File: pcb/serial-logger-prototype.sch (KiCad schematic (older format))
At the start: 52 parts, among them J1 Conn_ARM_JTAG_SWD_10, J2 Conn_01x04_Female, J3 Conn_01x04_Female, J4 Conn_01x03_Male, SW1 Rotary_Encoder_Switch_DualLED, SW2 SW_SPDT, U1 STM32G070KBT6, U2 74LVC3G17, U3 TLV70228_SOT23-5, U4 sn74lv1t34, U5 TLV61046ADB, U6 sn74lv1t34

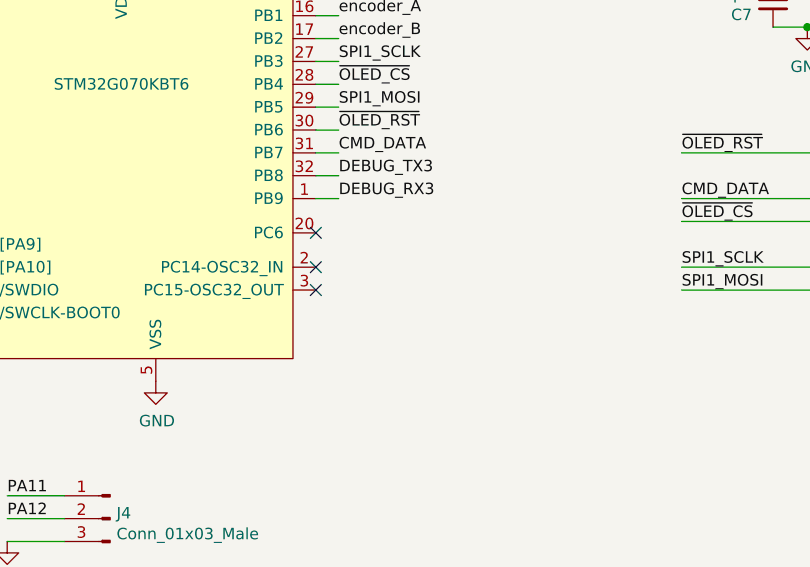
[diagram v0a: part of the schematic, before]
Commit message: Add note about PC13-15
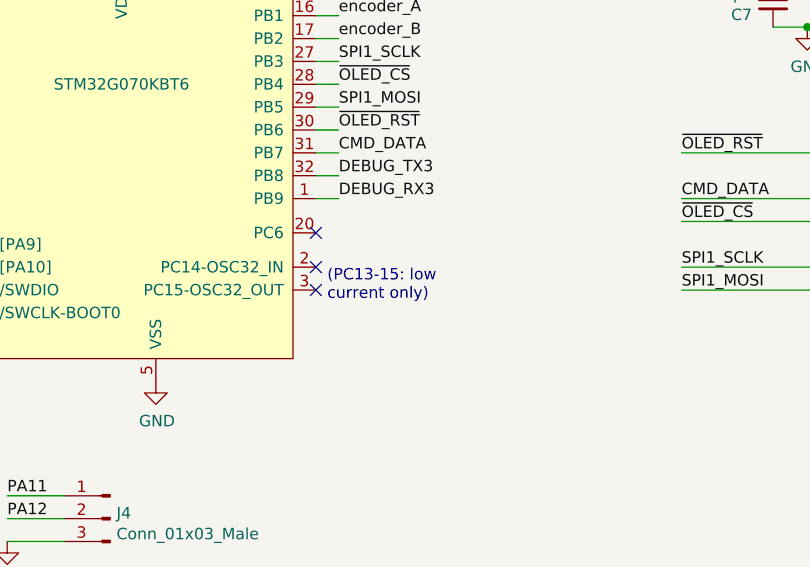
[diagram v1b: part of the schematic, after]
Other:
- note added: "(PC13-15: low\ncurrent only)"
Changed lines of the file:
@@
 	-1   0    0    -1
 $EndComp
+Text Notes 4850 3300 0    50   ~ 0
+(PC13-15: low\ncurrent only)
 $EndSCHEMATC

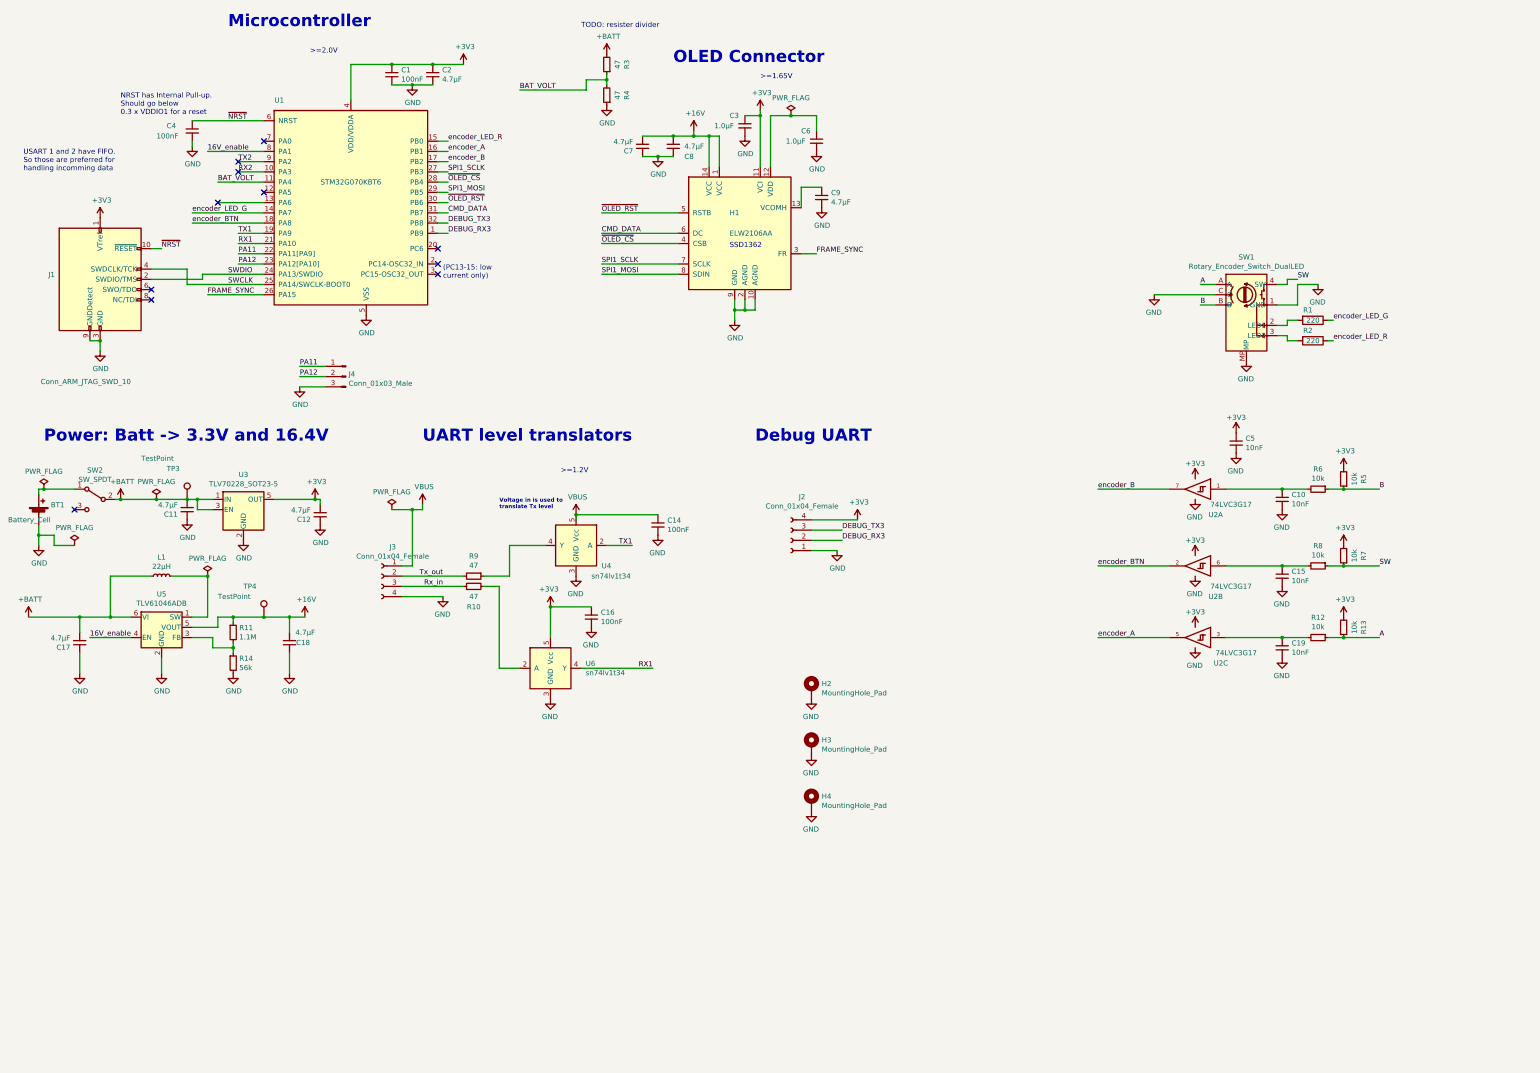
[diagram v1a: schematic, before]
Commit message: Schematics: implement BATT_VOLT, shuffle schematics blocks around
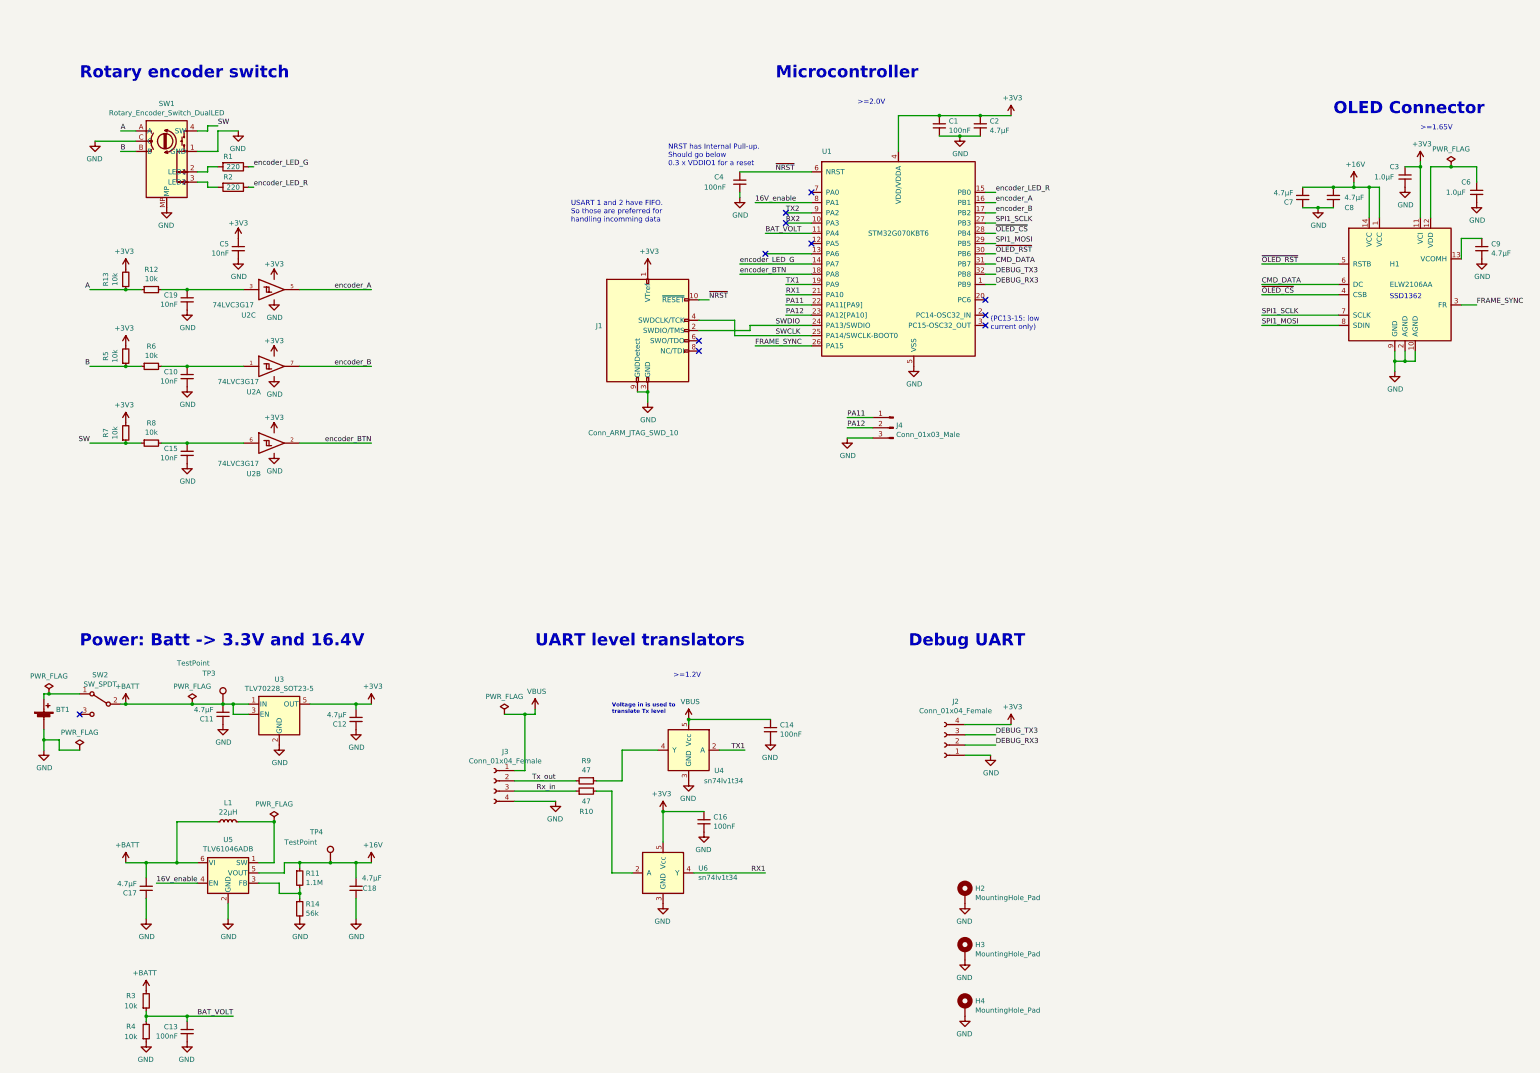
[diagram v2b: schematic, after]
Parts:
- added C13: 100nF, Capacitor_SMD:C_0402_1005Metric, symbol Device:C_Small
- C4: Reason (none) -> prevent parasitic resets (see datasheet 5.3.15)
- R3, R4: value 47 -> 10k
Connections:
- net BAT_VOLT: now also C13.1
- net GND: now also C13.2
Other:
- note added: "Rotary encoder switch"
- note removed: "TODO: resister divider"
- moved on the sheet: BT1, C1, C10, C11, C12, C14, C15, C16, C17, C18, C19, C2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

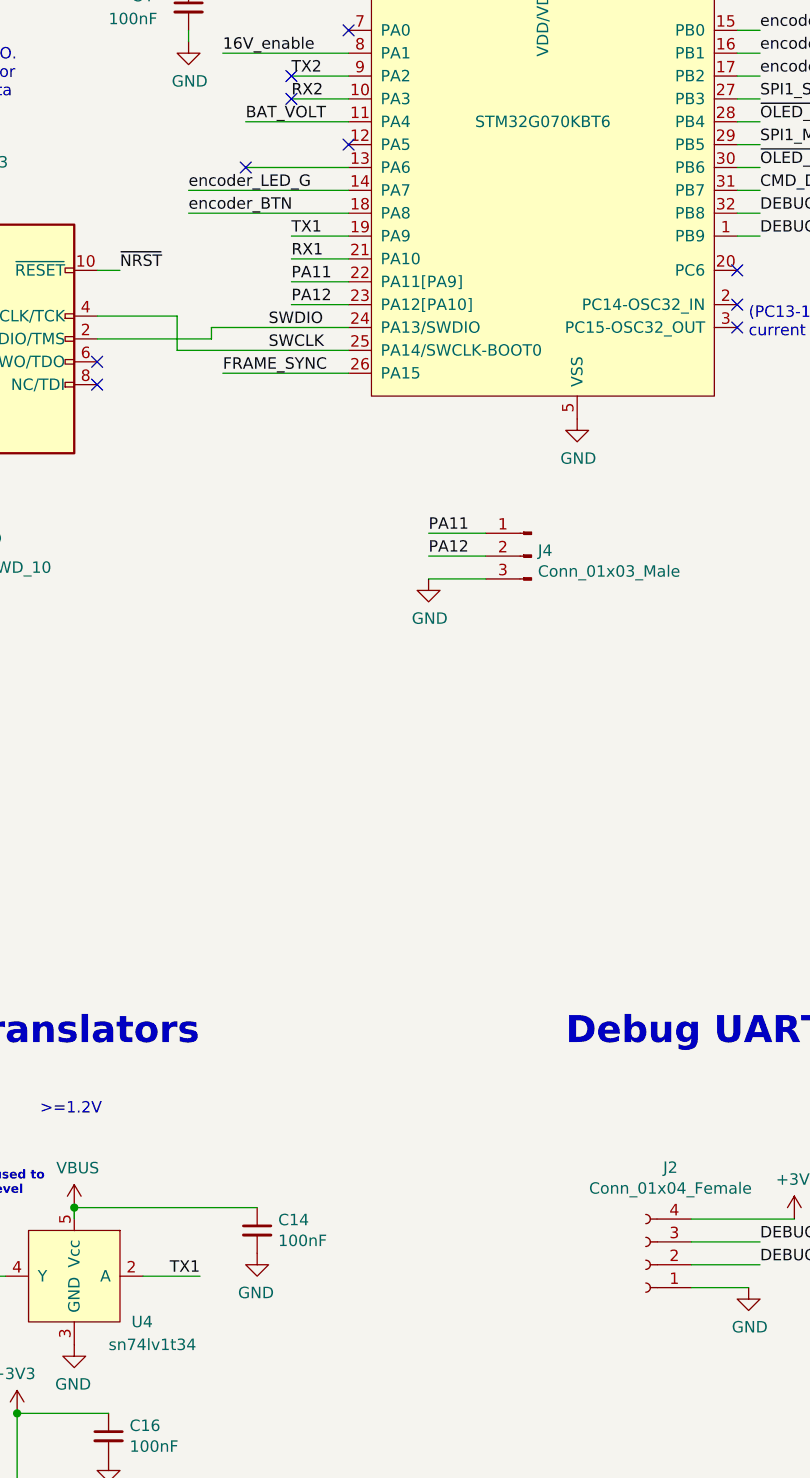
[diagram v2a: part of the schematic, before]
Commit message: PCB: cleanup layout, optimize for 3d enclosure
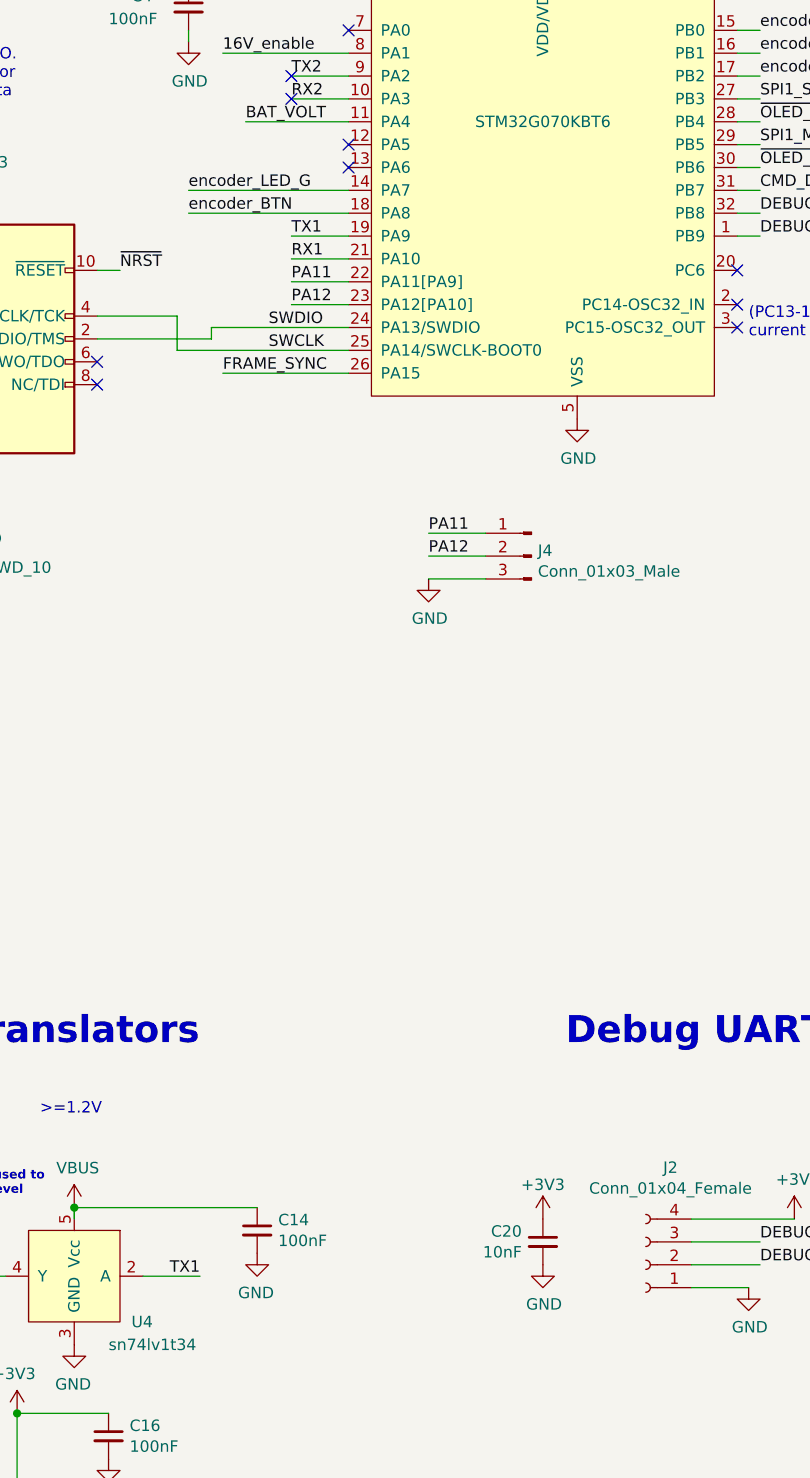
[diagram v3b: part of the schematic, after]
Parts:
- added C20: 10nF, Capacitor_SMD:C_0402_1005Metric, symbol Device:C_Small
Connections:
- net +3V3: now also C20.1
- net GND: now also C20.2
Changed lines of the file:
@@
 Text Label 10250 2950 0    50   ~ 0
 SPI1_MOSI
-Wire Wire Line
-	8000 3050 8450 3050
 $Comp
 L Device:C_Small C4
@@
 Wire Wire Line
 	7750 2450 7750 2500
-NoConn ~ 8000 3050
+NoConn ~ 8450 3050
 $Comp
 L power:GND #PWR035
@@
 	-1   0    0    -1
 $EndComp
+$Comp
+L Device:C_Small C20
+U 1 1 5E5CE5CC
+P 9300 7750
+F 0 "C20" H 9392 7796 50  0000 L CNN
+F 1 "10nF" H 9392 7705 50  0000 L CNN
+F 2 "Capacitor_SMD:C_0402_1005Metric" H 9300 7750 50  0001 C CNN
+F 3 "~" H 9300 7750 50  0001 C CNN
+	1    9300 7750
+	-1   0    0    -1
+$EndComp
+$Comp
+L power:GND #PWR0108
+U 1 1 5E5CE5D2
+P 9300 7850
+F 0 "#PWR0108" H 9300 7600 50  0001 C CNN
+F 1 "GND" H 9305 7677 50  0000 C CNN
+F 2 "" H 9300 7850 50  0001 C CNN
+F 3 "" H 9300 7850 50  0001 C CNN
+	1    9300 7850
+	1    0    0    -1
+$EndComp
+$Comp
+L power:+3V3 #PWR0109
+U 1 1 5E5CE5D8
+P 9300 7650
+F 0 "#PWR0109" H 9300 7500 50  0001 C CNN
+F 1 "+3V3" H 9300 7800 50  0000 C CNN
+F 2 "" H 9300 7650 50  0001 C CNN
+F 3 "" H 9300 7650 50  0001 C CNN
+	1    9300 7650
+	-1   0    0    -1
+$EndComp

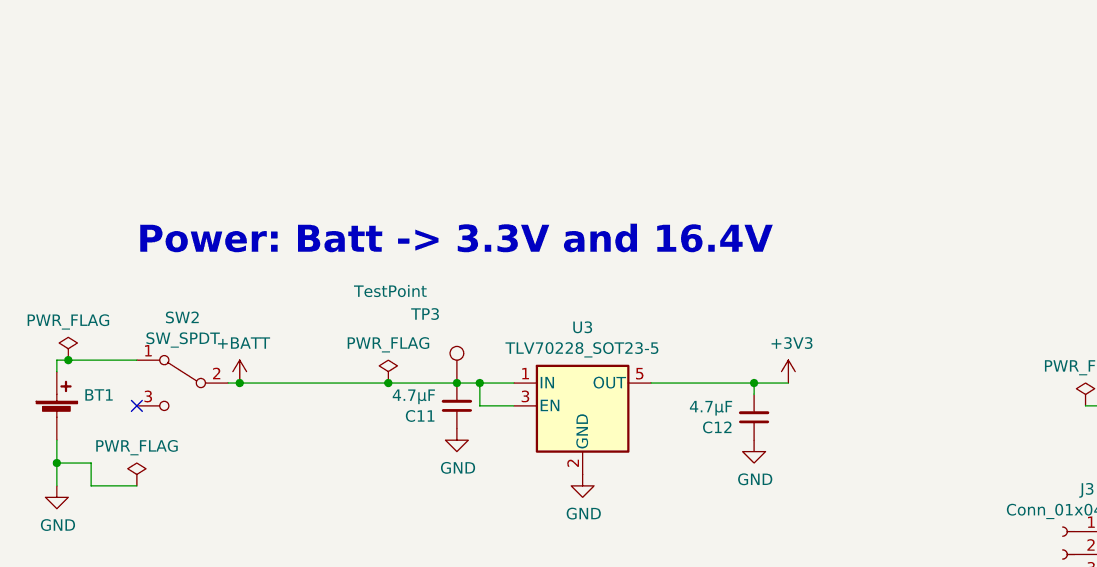
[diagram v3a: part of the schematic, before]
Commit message: PCB: tweak placements + silk screen
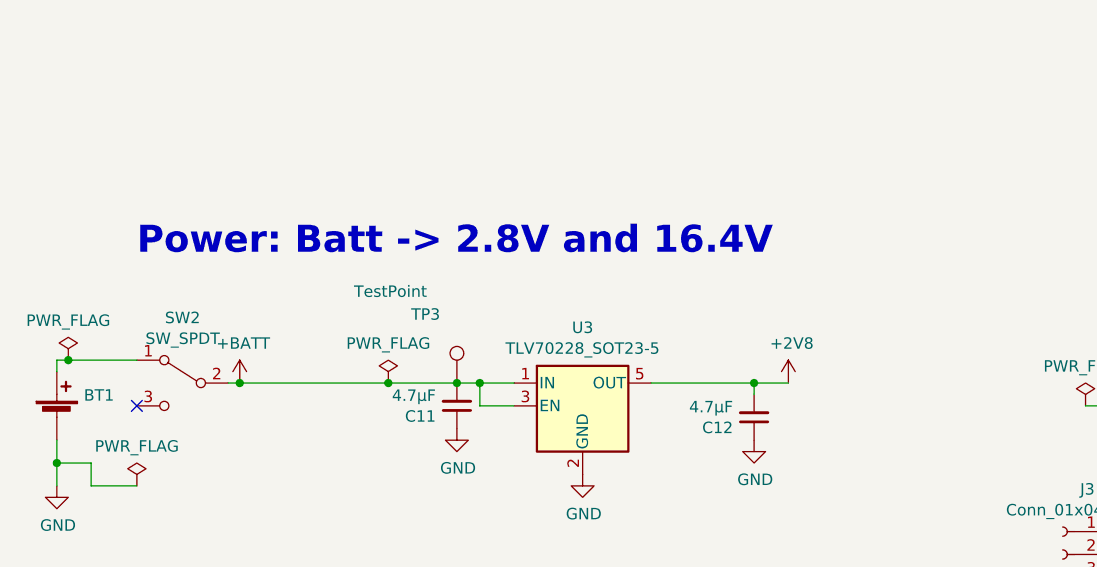
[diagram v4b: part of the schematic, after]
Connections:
- net +3V3: no longer C12.2, U3.5 (OUT)
- new net +2V8: C12.2, U3.5 (OUT)
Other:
- note added: "Power: Batt -> 2.8V and 16.4V"
- note removed: "Power: Batt -> 3.3V and 16.4V"
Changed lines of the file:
@@
 Microcontroller
 Text Notes 1300 6900 0    118  ~ 24
-Power: Batt -> 3.3V and 16.4V
+Power: Batt -> 2.8V and 16.4V
 Connection ~ 1750 7450
 Text Notes 5750 6900 0    118  ~ 24
@@
 	4150 7450 4000 7450
 $Comp
-L power:+3V3 #PWR022
-U 1 1 5E21DE1E
-P 4150 7450
-F 0 "#PWR022" H 4150 7300 50  0001 C CNN
-F 1 "+3V3" H 4165 7623 50  0000 C CNN
-F 2 "" H 4150 7450 50  0001 C CNN
-F 3 "" H 4150 7450 50  0001 C CNN
-	1    4150 7450
-	1    0    0    -1
-$EndComp
-$Comp
 L power:+3V3 #PWR014
 U 1 1 5E286E0A
@@
 	-1   0    0    -1
 $EndComp
+$Comp
+L power:+2V8 #PWR?
+U 1 1 5E3BE60D
+P 4150 7450
+F 0 "#PWR?" H 4150 7300 50  0001 C CNN
+F 1 "+2V8" H 4165 7623 50  0000 C CNN
+F 2 "" H 4150 7450 50  0001 C CNN
+F 3 "" H 4150 7450 50  0001 C CNN
+	1    4150 7450
+	1    0    0    -1
+$EndComp
 $EndSCHEMATC

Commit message: PCB: finalize design (DRC pass)
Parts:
- added MB1, MB2, MB3, MB4: MouseBite, Jitter_Footprints:MouseBite_3.5mmx2.2mm_breakaway, symbol Mechanical:MountingHole
- added TH? (x4): ToolingHole, Jitter_Footprints:Tooling_hole_4mm_4.04mm_paste, symbol Mechanical:MountingHole
- added TP1, TP2, TP5, TP6, TP7, TP8, TP9: TestPoint, TestPoint:TestPoint_Pad_D1.0mm, symbol Connector:TestPoint
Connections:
- net +3V3 is gone; now on net +2V8: C1.1, C16.1, C2.1, C20.1, C3.1, C5.1, H1.11 (VCI), J1.1 (VTref), J2.4 (Pin_4), R13.2, R5.2, R7.2, U1.4 (VDD/VDDA), U2.8 (VCC), U2.8 (VCC), U2.8 (VCC), U6.5 (Vcc)
- net CMD_DATA: now also TP7.1
- net FRAME_SYNC: now also TP9.1
- net RX1: now also TP2.1
- net SPI1_MOSI: now also TP6.1
- net SPI1_SCLK: now also TP5.1
- net TX1: now also TP1.1
- net ~OLED_CS: now also TP8.1
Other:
- note added: "Test points"
- moved on the sheet: C14

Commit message: Schematics: annotate
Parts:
- gave numbers to parts that had none: 4
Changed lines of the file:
@@
 $EndComp
 $Comp
-L Mechanical:MountingHole TH?
+L Mechanical:MountingHole TH2
 U 1 1 5E4D8439
 P 8850 9750
-F 0 "TH?" H 8950 9750 50  0000 L CNN
+F 0 "TH2" H 8950 9750 50  0000 L CNN
 F 1 "ToolingHole" H 8950 9705 50  0001 L CNN
 F 2 "Jitter_Footprints:Tooling_hole_4mm_4.04mm_paste" H 8850 9750 50  0001 C CNN
@@
 $EndComp
 $Comp
-L Mechanical:MountingHole TH?
+L Mechanical:MountingHole TH1
 U 1 1 5E4D8C2B
 P 8850 9550
-F 0 "TH?" H 8950 9550 50  0000 L CNN
+F 0 "TH1" H 8950 9550 50  0000 L CNN
 F 1 "ToolingHole" H 8950 9505 50  0001 L CNN
 F 2 "Jitter_Footprints:Tooling_hole_4mm_4.04mm_paste" H 8850 9550 50  0001 C CNN
@@
 $EndComp
 $Comp
-L Mechanical:MountingHole TH?
+L Mechanical:MountingHole TH3
 U 1 1 5E4D8CE5
 P 8850 9950
-F 0 "TH?" H 8950 9950 50  0000 L CNN
+F 0 "TH3" H 8950 9950 50  0000 L CNN
 F 1 "ToolingHole" H 8950 9905 50  0001 L CNN
 F 2 "Jitter_Footprints:Tooling_hole_4mm_4.04mm_paste" H 8850 9950 50  0001 C CNN
@@
 $EndComp
 $Comp
-L Mechanical:MountingHole TH?
+L Mechanical:MountingHole TH4
 U 1 1 5E4D8E27
 P 8850 10150
-F 0 "TH?" H 8950 10150 50  0000 L CNN
+F 0 "TH4" H 8950 10150 50  0000 L CNN
 F 1 "ToolingHole" H 8950 10105 50  0001 L CNN
 F 2 "Jitter_Footprints:Tooling_hole_4mm_4.04mm_paste" H 8850 10150 50  0001 C CNN
